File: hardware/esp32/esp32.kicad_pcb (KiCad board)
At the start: 4 copper layers, 50 x 50 mm, 63 parts, among them J1 Screw_Terminal_01x02, J2 ESP_left, J3 ESP_right, Q1 MMBT5401, Q2 MMBT2222A, U2 LMV321, U3 LMV321, U4 mini_esp32, U5 HT7533-1, U6 LM393

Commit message: Work on V3.1
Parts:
- removed U5: HT7533-1, Library:SOT-89-3
- added D2: SS14, Library:D_SMA, F.Cu at (122.7, 104.6)
- added J4: PlugIn_Terminal_01x02, Library:steckklemme2x1_dnp, F.Cu at (117.0, 111.8)
- added J5: Plugged into C8387, Library:nofoorprint, F.Cu at (153.5, 109.4)
- added S1: SYM_ESD_Small, Library:ESD-Logo_6.6x6mm_SilkScreen, B.Cu at (123.4, 89.5)
- C11, C13, C15, C16, C17, C5, C6, C7: footprint Library:C_0603_1608Metric_Pad1.08x0.95mm_HandSolder -> Library:C_0402_1005Metric_Pad0.74x0.62mm_HandSolder
- C3: value 10n -> 100n; footprint Library:C_0603_1608Metric_Pad1.08x0.95mm_HandSolder -> Library:C_0402_1005Metric_Pad0.74x0.62mm_HandSolder
- J1: value Screw_Terminal_01x02 -> PlugIn_Terminal_01x02; footprint Library:anschlussklemme2x1 -> Library:steckklemme2x1_1
- R13, R29, R31, R8: footprint Library:R_0603_1608Metric_Pad0.98x0.95mm_HandSolder -> Library:R_0402_1005Metric_Pad0.72x0.64mm_HandSolder
- U4: value mini_esp32 -> ~
- moved C10 34.4 mm to (129.1, 98.2), turned to 90 degrees
- moved C9 33.9 mm to (126.1, 98.2)
- moved R21 33.4 mm to (127.2, 95.7), turned to 0 degrees
- moved C7 31.1 mm to (125.4, 92.3), turned to 180 degrees
- moved R34 30.9 mm to (127.2, 94.2), turned to 180 degrees
- moved C8 30.9 mm to (124.6, 98.2)
- moved R15 30.8 mm to (122.0, 101.0)
- moved R19 30.8 mm to (123.8, 93.9)
- moved R18 30.6 mm to (123.8, 95.4)
- moved R20 30.5 mm to (127.6, 98.2)
- moved U3 30.3 mm to (122.1, 98.2)
- moved R17 29.9 mm to (120.5, 93.9)
- moved R16 29.8 mm to (120.5, 95.4)
- moved R14 29.7 mm to (119.6, 98.2)
- moved Q1 28.2 mm to (130.0, 81.3), turned to 0 degrees
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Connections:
- D1 pad 3: Net-(J1-Pin_1) -> Net-(J1-Pin_2)
- D1 pad 4: Net-(J1-Pin_2) -> Net-(J1-Pin_1)
- J2 pad 16: unconnected-(J2-3V3-Pad16) -> +3.3V
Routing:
- net GND: track 32.8 -> 2.02 mm, vias 54 -> 19
- net +5V: track 26.6 -> 13.5 mm, vias 5 -> 6
- net Net-(D2-A): track 0.00 -> 7.86 mm
- net Net-(D1-+): track 5.51 -> 13.0 mm, vias 0 -> 2
- net +3.3V: track 24.2 -> 17.3 mm, vias 10 -> 7
- net /5V_onoff: track 12.8 -> 7.66 mm
- net Net-(R11-Pad1): track 16.8 -> 21.2 mm, vias 0 -> 2
- net /TX: track 17.4 -> 21.1 mm, vias 0 -> 2
- net Net-(U1-+): track 6.59 -> 2.96 mm
- net Net-(C2-Pad2): track 8.10 -> 4.68 mm
- net Net-(J1-Pin_2): track 13.4 -> 10.1 mm
- net /RX_ANA: track 27.7 -> 24.4 mm, vias 0 -> 1
- net /RX: track 22.3 -> 25.3 mm
- net Net-(U2-+): track 7.69 -> 4.80 mm
- net /RX_DAC: track 20.1 -> 22.6 mm
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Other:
- board size 50 x 50 mm -> 32.8 x 36.3 mm
- board text added: "5V PWR in"
- board text added: "A"
- board text added: "Bus"
- board text added: "ESP 3.3Vout"
- board text added: "ESP 5Vout"
- board text added: "ESP32Mini"
- board text added: "PWR IN: 5V, 1A"
- board text added: "github.com/ gdoor-org/gdoor"
- board text added: "max. 40V"
- board text added: "max. 6V"
- board text added: "⚠"
- board text removed: "*) Debug Pins"
- board text removed: "5Vin"
- board text removed: "5Vin: max. 6V, 100mA"
- board text removed: "Analog in: RX_THRESH* (0-3.3V)"
- board text removed: "Analog out: RX_ANA* (0-3.3V)"
- board text removed: "Bus A"
- board text removed: "Bus B"
- board text removed: "Door Bus"
- board text removed: "ESP32 mini"
- board text removed: "GPIO in: TX, TX_EN"
- board text removed: "GPIO out: RX, RX_DAC*"
- board text removed: "I1"
- board text removed: "I2"
- board text removed: "T"
- board text removed: "https://github.com/gdoor-org/gdoor"
- board text removed: "max. 40Vdc"

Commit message: Work on V3.1
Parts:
- moved C15 12.3 mm to (125.6, 101.1), turned to 0 degrees
- moved J1 0.42 mm to (138.2, 109.7)
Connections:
- C15 pad 1: +5V -> +5Vonoff
- C3 pad 1: /5V_onoff -> +5Vonoff
- C7 pad 1: /5V_onoff -> +5Vonoff
- Q1 pad 3: /5V_onoff -> +5Vonoff
- R17 pad 1: /5V_onoff -> +5Vonoff
- R18 pad 2: /5V_onoff -> +5Vonoff
- R33 pad 1: /5V_onoff -> +5Vonoff
- U pad 5: /5V_onoff -> +5Vonoff
- U3 pad 5: /5V_onoff -> +5Vonoff
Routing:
- net +5Vonoff: track 0.00 -> 8.49 mm, vias 0 -> 8
- net /5V_onoff: track 7.66 -> 0.00 mm, vias 7 -> 0
- net +5V: track 13.5 -> 11.7 mm
- added copper zone on In2.Cu, net +5Vonoff
- removed copper zone on In2.Cu, net /5V_onoff

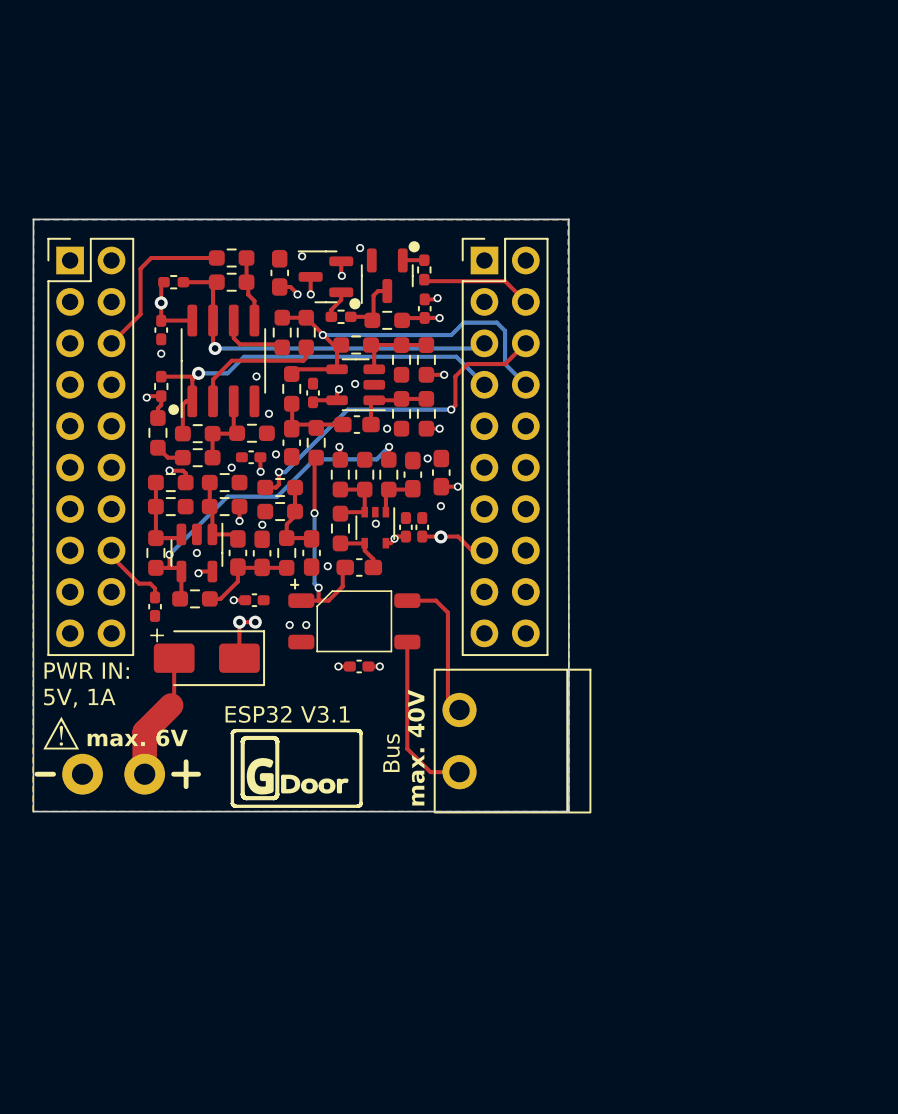
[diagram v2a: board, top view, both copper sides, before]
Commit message: V3.1: Add power filtering
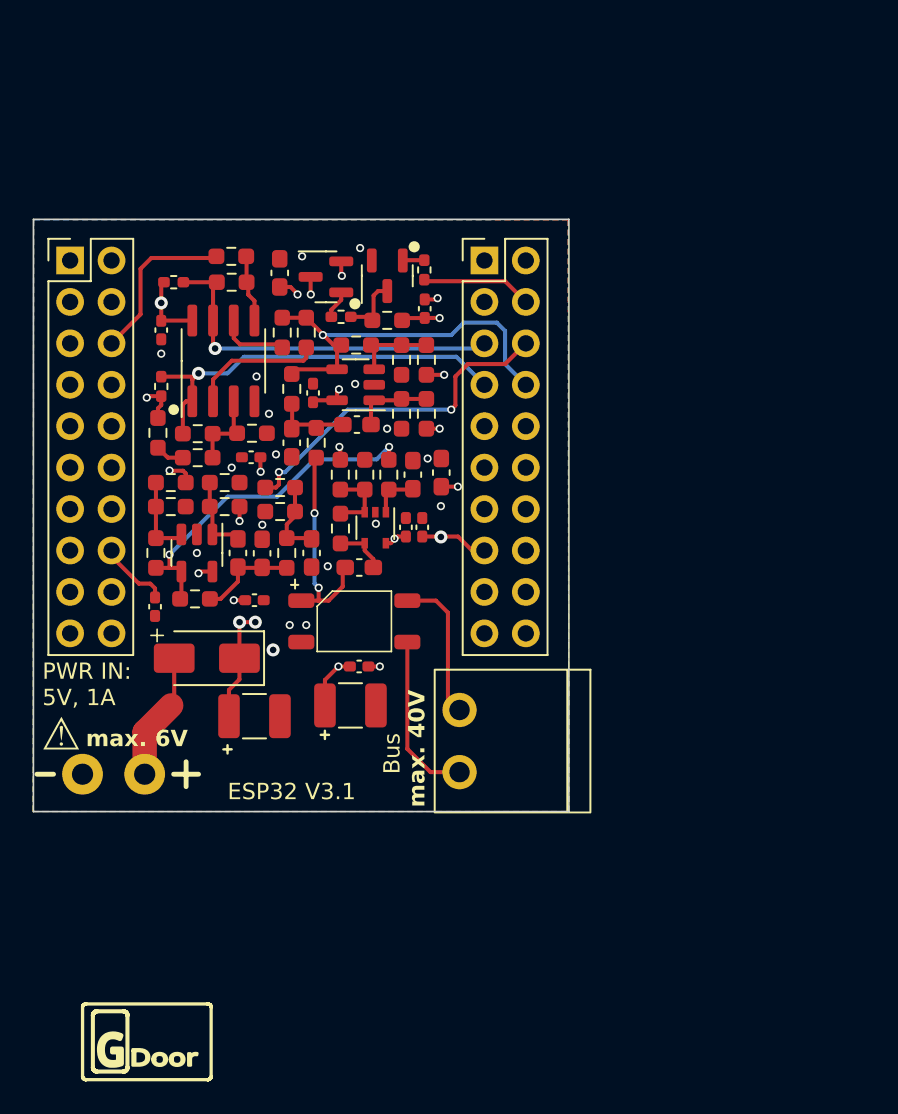
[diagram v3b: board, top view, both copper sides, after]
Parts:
- removed R32: 2k4, Library:R_0603_1608Metric_Pad0.98x0.95mm_HandSolder
- added C19: 100u, Library:C_1210_3225Metric_Pad1.33x2.70mm_HandSolder, F.Cu at (131.5, 107.5)
- added C20: 100u, Library:C_1210_3225Metric_Pad1.33x2.70mm_HandSolder, F.Cu at (125.6, 108.2)
- added R22: 18k, Library:R_0603_1608Metric_Pad0.98x0.95mm_HandSolder, F.Cu at (124.2, 80.0)
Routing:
- net +5V: track 11.7 -> 15.5 mm
- net +3.3V: track 17.3 -> 20.1 mm
- net GND: vias 19 -> 20

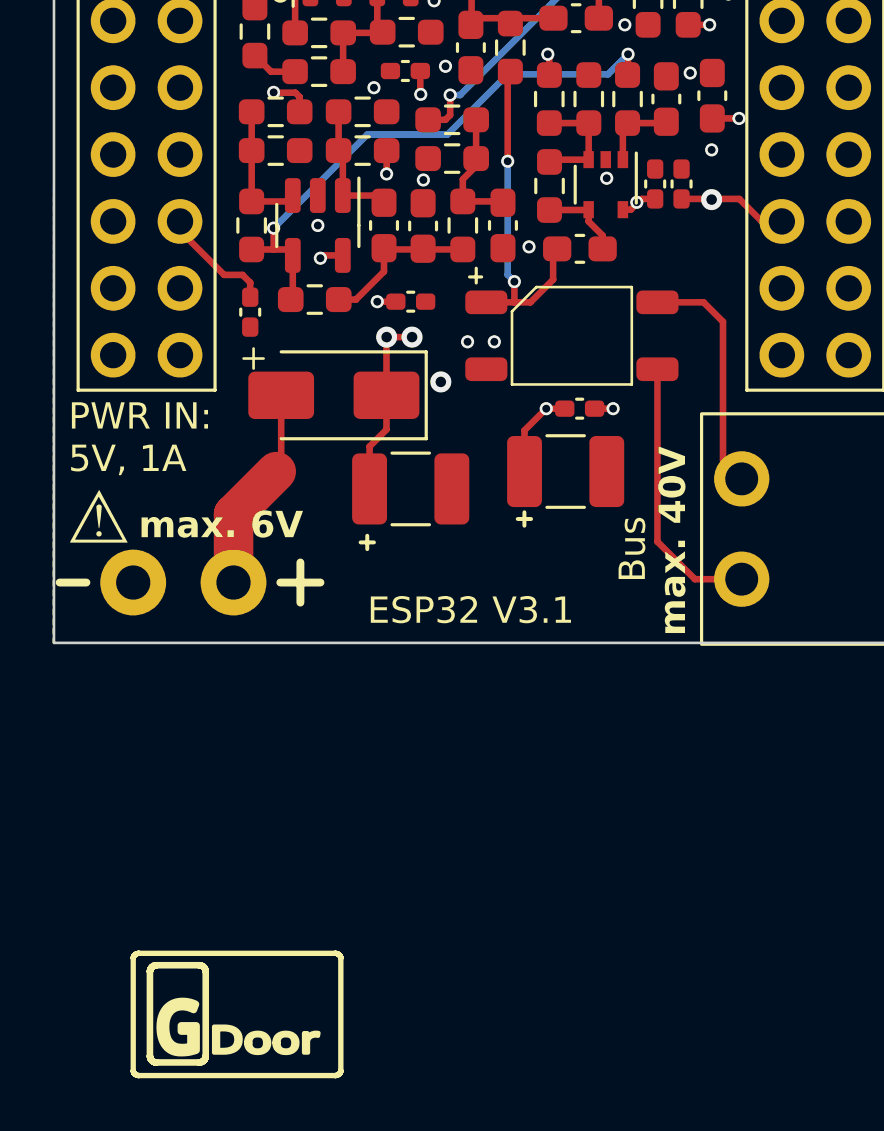
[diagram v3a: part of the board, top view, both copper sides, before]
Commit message: add 100k on hw v3.1
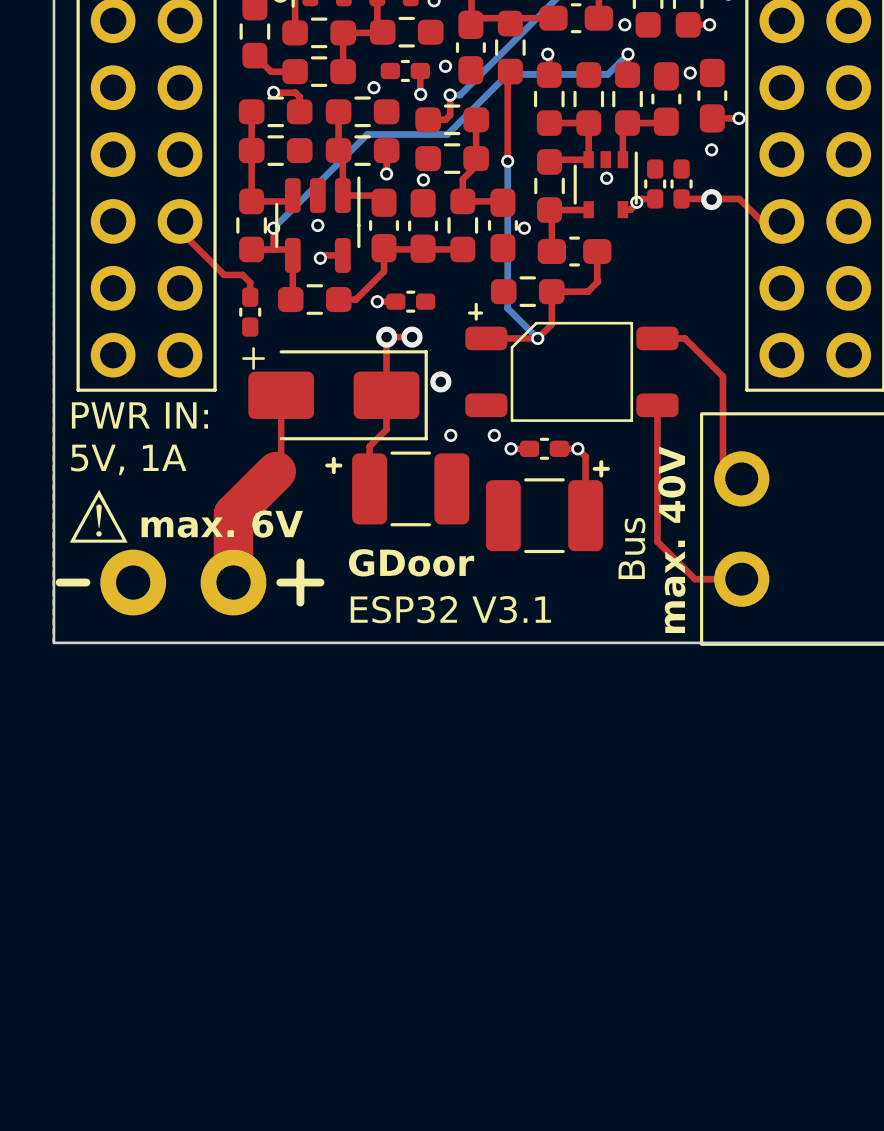
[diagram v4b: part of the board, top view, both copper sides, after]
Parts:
- added R32: 100k, Library:R_0603_1608Metric_Pad0.98x0.95mm_HandSolder, F.Cu at (130.0, 100.7)
- moved C13 2.03 mm to (130.7, 106.7), turned to 0 degrees
- moved C19 1.86 mm to (130.7, 109.2), turned to 180 degrees
- moved D1 1.37 mm to (131.7, 103.8)
- moved C1 0.23 mm to (131.8, 99.2), turned to 0 degrees
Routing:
- net Net-(D1-+): track 13.0 -> 17.7 mm
- net Net-(J1-Pin_1): track 9.06 -> 7.27 mm
- net Net-(J1-Pin_2): track 10.3 -> 8.97 mm
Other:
- board text added: "Connector C8466 (J5) plugged into C8387 (J1)"
- board text added: "GDoor"
- board text added: "J1"
- board text added: "J5"
- board text added: "gdoor-org.github.io"
- board text removed: "github.com/ gdoor-org/gdoor"
